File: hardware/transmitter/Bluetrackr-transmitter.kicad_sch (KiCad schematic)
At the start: 43 parts, among them J1 USB_C_Receptacle_USB2.0, J2 Programming_Connector, J3 Battery_Connector, Q1 CJ2333, SW1 SW_Pair, U1 MCP73831-2-OT, U2 MIC5205-2.5YM5, U4 STM32F030R8Tx

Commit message: Annotate schematic
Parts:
- gave numbers to parts that had none: 7
- renumbered C4 to C1, C13 to C10, C14 to C11, C9 to C12, C5 to C2, C2 to C3, C6 to C4, C1 to C5, C3 to C6, C10 to C7, C11 to C8, C12 to C9, R4 to R1, R5 to R2, R6 to R3, R1 to R4, R2 to R5, R3 to R6, U2 to U1, U1 to U2, U4 to U3

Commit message: Remove pcb
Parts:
- C12: footprint Capacitor_SMD:CP_Elec_4x5.4 -> Capacitor_SMD:CP_Elec_3x5.3
- C13, C14, C16, C17: footprint (none) -> Capacitor_SMD:C_0805_2012Metric_Pad1.15x1.40mm_HandSolder
- C15: footprint (none) -> Capacitor_SMD:CP_Elec_3x5.3
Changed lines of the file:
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@@
       (effects (font (size 1.27 1.27)) (justify left))
     )
-    (property "Footprint" "Capacitor_SMD:CP_Elec_4x5.4" (id 2) (at 205.4352 55.88 0)
+    (property "Footprint" "Capacitor_SMD:CP_Elec_3x5.3" (id 2) (at 205.4352 55.88 0)
       (effects (font (size 1.27 1.27)) hide)
     )
@@
       (effects (font (size 1.27 1.27)) (justify left))
     )
-    (property "Footprint" "" (id 2) (at 285.4452 85.09 0)
+    (property "Footprint" "Capacitor_SMD:C_0805_2012Metric_Pad1.15x1.40mm_HandSolder" (id 2) (at 285.4452 85.09 0)
       (effects (font (size 1.27 1.27)) hide)
     )
@@
       (effects (font (size 1.27 1.27)) (justify left))
     )
-    (property "Footprint" "" (id 2) (at 300.6852 85.09 0)
+    (property "Footprint" "Capacitor_SMD:C_0805_2012Metric_Pad1.15x1.40mm_HandSolder" (id 2) (at 300.6852 85.09 0)
       (effects (font (size 1.27 1.27)) hide)
     )
@@
       (effects (font (size 1.27 1.27)) (justify left))
     )
-    (property "Footprint" "" (id 2) (at 305.7652 118.11 0)
+    (property "Footprint" "Capacitor_SMD:CP_Elec_3x5.3" (id 2) (at 305.7652 118.11 0)
       (effects (font (size 1.27 1.27)) hide)
     )
@@
       (effects (font (size 1.27 1.27)) (justify left))
     )
-    (property "Footprint" "" (id 2) (at 315.9252 118.11 0)
+    (property "Footprint" "Capacitor_SMD:C_0805_2012Metric_Pad1.15x1.40mm_HandSolder" (id 2) (at 315.9252 118.11 0)
       (effects (font (size 1.27 1.27)) hide)
     )
@@
       (effects (font (size 1.27 1.27)) (justify left))
     )
-    (property "Footprint" "" (id 2) (at 327.3552 118.11 0)
+    (property "Footprint" "Capacitor_SMD:C_0805_2012Metric_Pad1.15x1.40mm_HandSolder" (id 2) (at 327.3552 118.11 0)
       (effects (font (size 1.27 1.27)) hide)
     )

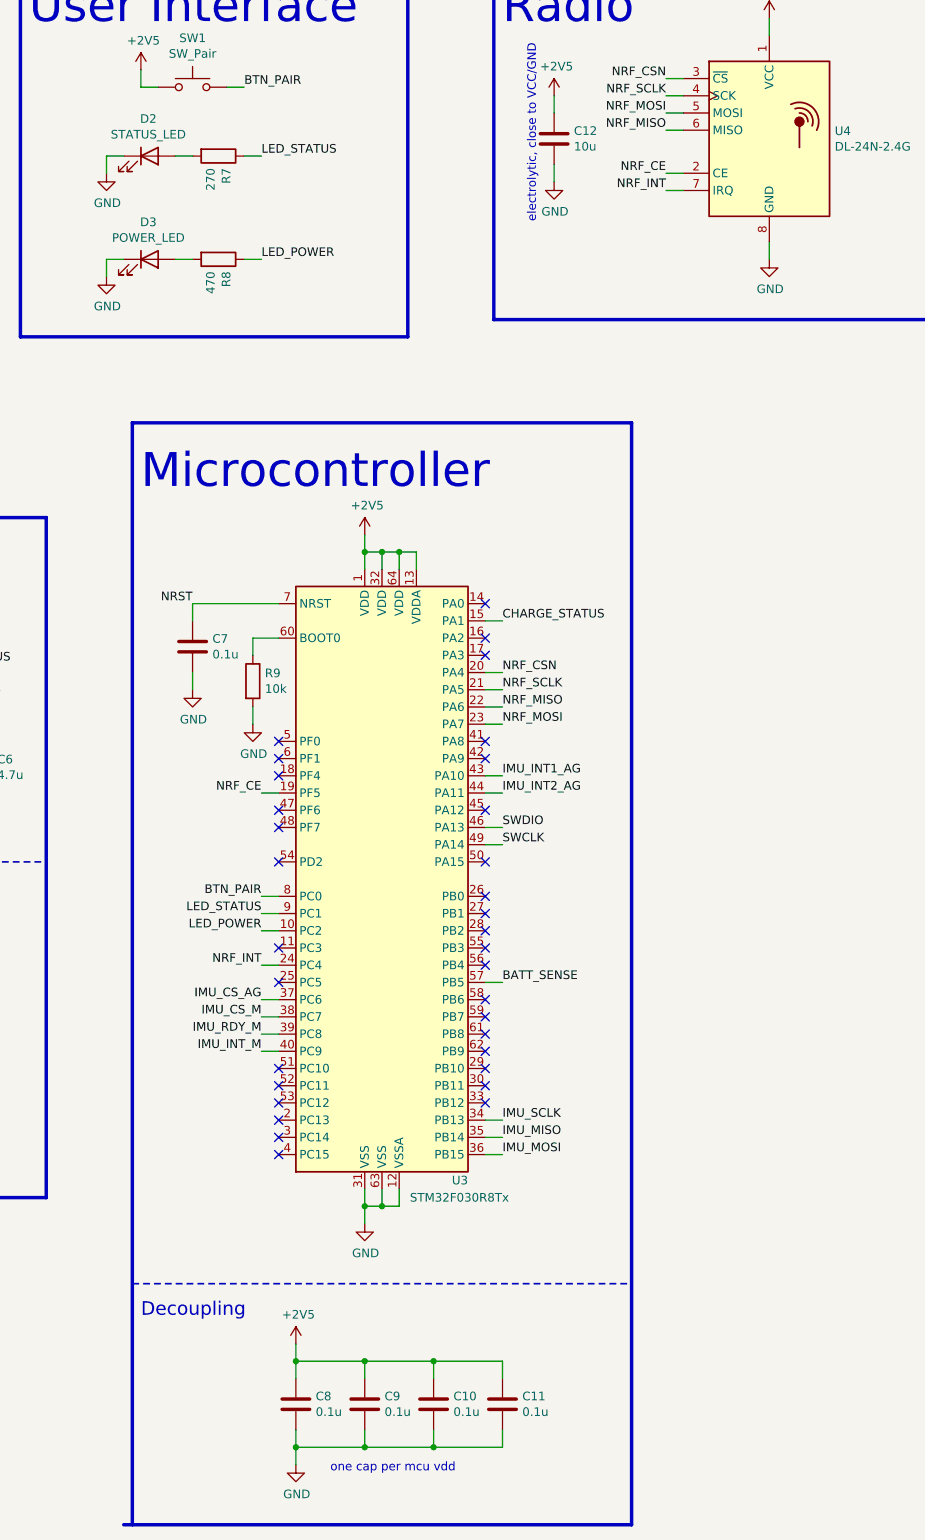
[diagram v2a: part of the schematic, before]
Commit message: Finish schematic with new Radio & IMU
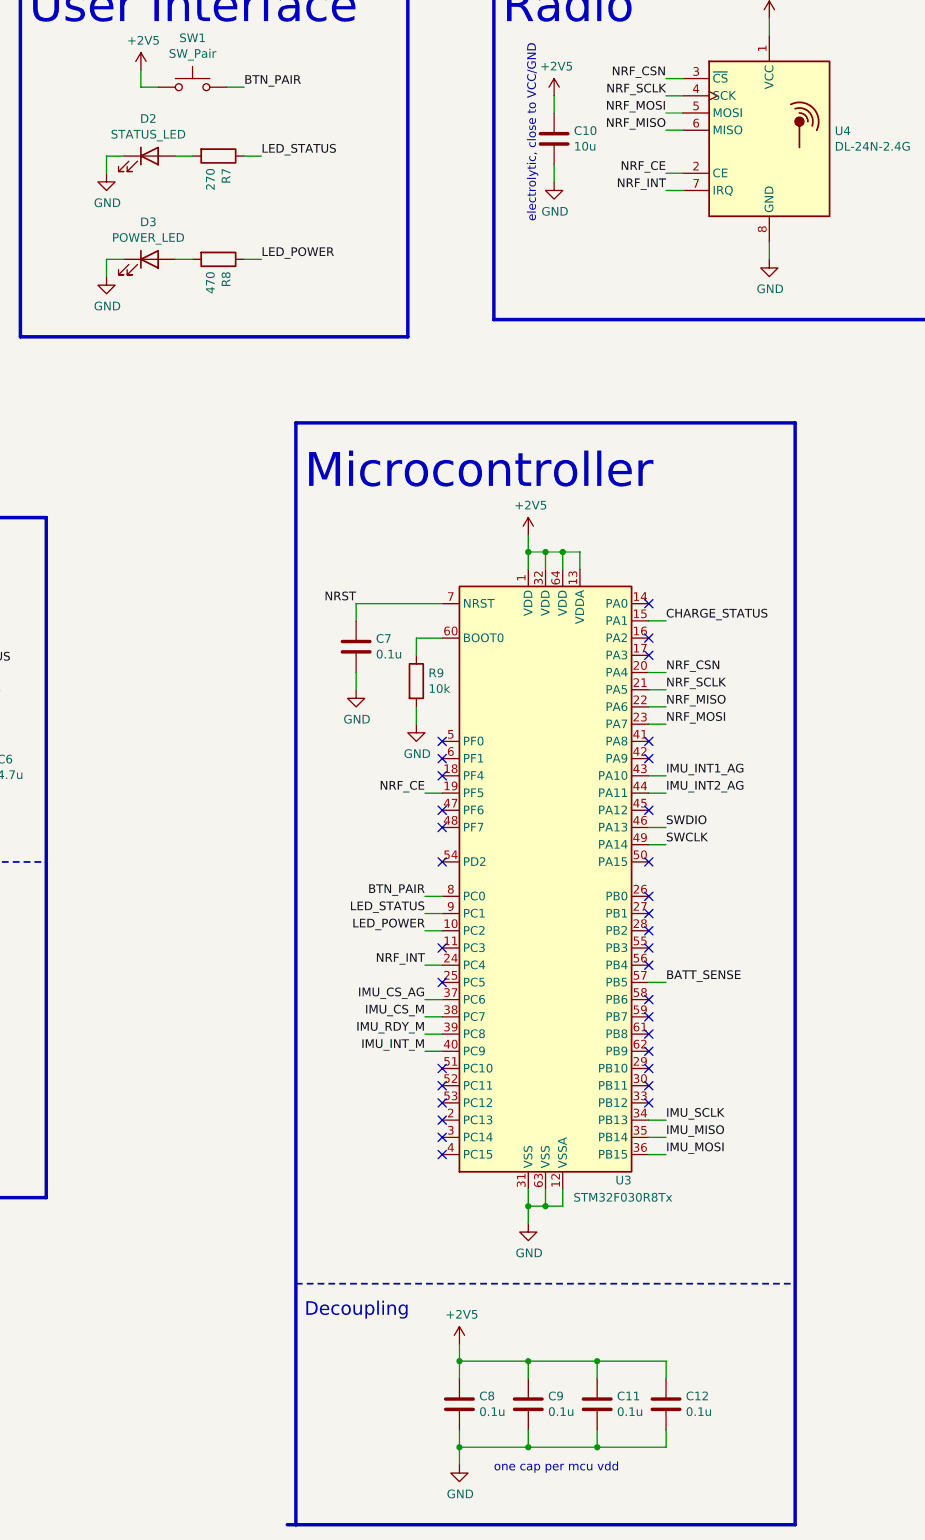
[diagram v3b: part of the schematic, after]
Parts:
- renumbered C12 to C10, C10 to C11, C11 to C12
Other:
- moved on the sheet: C11, C12, C7, C8, C9, R9, U3

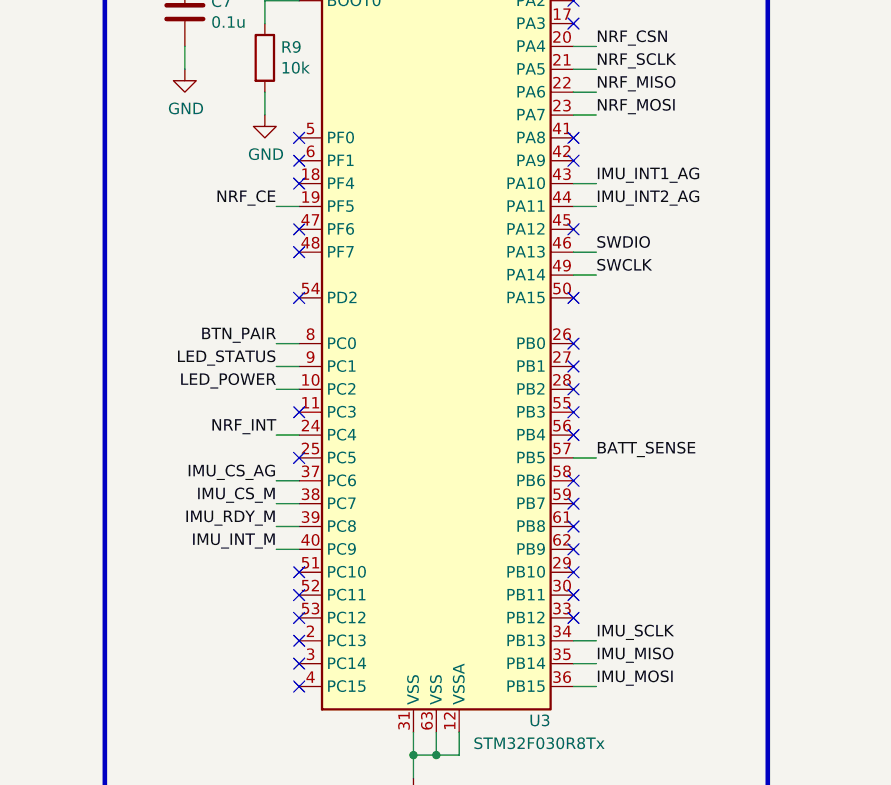
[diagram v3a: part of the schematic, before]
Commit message: Changed MCU to IMU pins
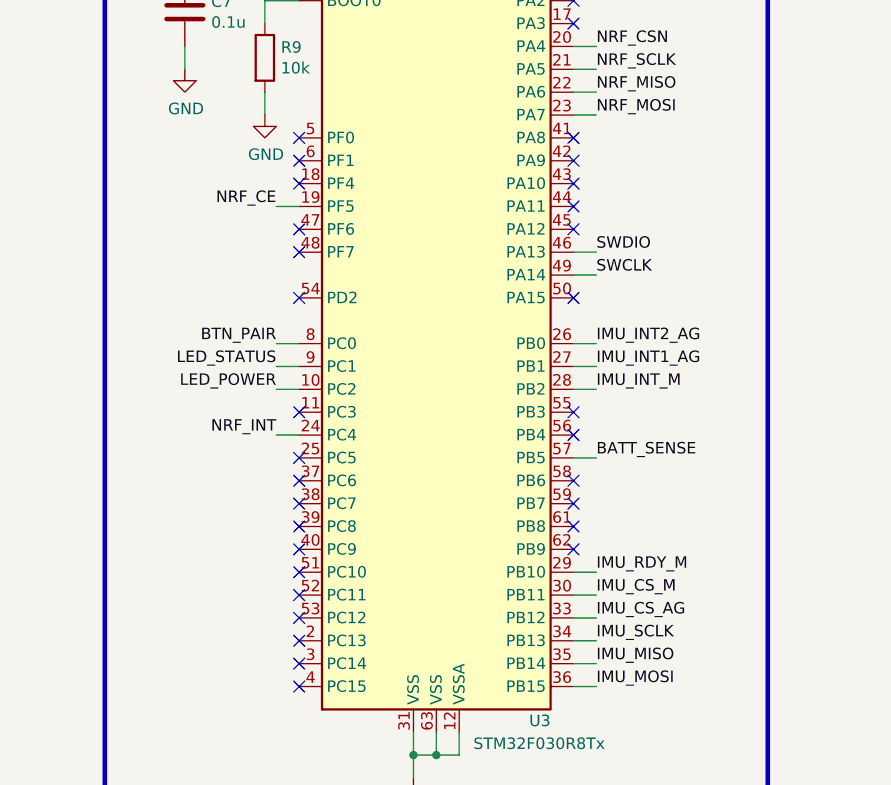
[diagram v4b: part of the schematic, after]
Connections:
- net IMU_CS_AG: now also U3.33 (PB12); no longer U3.37 (PC6)
- net IMU_CS_M: now also U3.30 (PB11); no longer U3.38 (PC7)
- net IMU_INT1_AG: now also U3.27 (PB1); no longer U3.43 (PA10)
- net IMU_INT2_AG: now also U3.26 (PB0); no longer U3.44 (PA11)
- net IMU_INT_M: now also U3.28 (PB2); no longer U3.40 (PC9)
- net IMU_RDY_M: now also U3.29 (PB10); no longer U3.39 (PC8)
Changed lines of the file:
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@@
   (junction (at 340.36 69.85))
   (junction (at 340.36 72.39))
-  (no_connect (at 218.44 189.23))
+  (no_connect (at 218.44 125.73))
+  (no_connect (at 187.96 196.85))
+  (no_connect (at 218.44 158.75))
+  (no_connect (at 54.61 58.42))
+  (no_connect (at 187.96 189.23))
+  (no_connect (at 187.96 153.67))
+  (no_connect (at 187.96 146.05))
+  (no_connect (at 187.96 140.97))
+  (no_connect (at 218.44 184.15))
+  (no_connect (at 218.44 186.69))
   (no_connect (at 218.44 151.13))
+  (no_connect (at 187.96 143.51))
+  (no_connect (at 54.61 60.96))
+  (no_connect (at 187.96 194.31))
+  (no_connect (at 218.44 181.61))
+  (no_connect (at 187.96 171.45))
+  (no_connect (at 218.44 143.51))
+  (no_connect (at 218.44 140.97))
+  (no_connect (at 187.96 191.77))
+  (no_connect (at 187.96 158.75))
+  (no_connect (at 54.61 66.04))
+  (no_connect (at 187.96 179.07))
+  (no_connect (at 187.96 181.61))
+  (no_connect (at 187.96 184.15))
+  (no_connect (at 187.96 186.69))
+  (no_connect (at 218.44 146.05))
+  (no_connect (at 218.44 148.59))
+  (no_connect (at 302.26 67.31))
+  (no_connect (at 54.61 63.5))
+  (no_connect (at 187.96 201.93))
   (no_connect (at 54.61 76.2))
-  (no_connect (at 187.96 153.67))
-  (no_connect (at 218.44 186.69))
+  (no_connect (at 218.44 128.27))
+  (no_connect (at 187.96 176.53))
+  (no_connect (at 218.44 171.45))
+  (no_connect (at 187.96 199.39))
+  (no_connect (at 187.96 151.13))
+  (no_connect (at 218.44 179.07))
+  (no_connect (at 218.44 120.65))
   (no_connect (at 54.61 73.66))
-  (no_connect (at 187.96 171.45))
-  (no_connect (at 187.96 201.93))
-  (no_connect (at 187.96 194.31))
-  (no_connect (at 218.44 191.77))
-  (no_connect (at 302.26 67.31))
-  (no_connect (at 187.96 176.53))
-  (no_connect (at 54.61 58.42))
-  (no_connect (at 187.96 191.77))
-  (no_connect (at 218.44 140.97))
-  (no_connect (at 187.96 158.75))
-  (no_connect (at 218.44 158.75))
-  (no_connect (at 187.96 140.97))
-  (no_connect (at 218.44 166.37))
-  (no_connect (at 218.44 120.65))
-  (no_connect (at 218.44 128.27))
-  (no_connect (at 54.61 63.5))
-  (no_connect (at 218.44 181.61))
-  (no_connect (at 218.44 163.83))
-  (no_connect (at 187.96 146.05))
-  (no_connect (at 218.44 194.31))
-  (no_connect (at 218.44 125.73))
-  (no_connect (at 218.44 168.91))
-  (no_connect (at 218.44 143.51))
-  (no_connect (at 187.96 199.39))
-  (no_connect (at 218.44 179.07))
-  (no_connect (at 187.96 151.13))
-  (no_connect (at 187.96 189.23))
-  (no_connect (at 218.44 184.15))
   (no_connect (at 218.44 173.99))
-  (no_connect (at 54.61 60.96))
-  (no_connect (at 187.96 143.51))
-  (no_connect (at 218.44 171.45))
-  (no_connect (at 54.61 66.04))
-  (no_connect (at 187.96 196.85))
   (wire (pts (xy 30.48 129.54) (xy 30.48 132.08))
     (stroke (width 0) (type solid) (color 0 0 0 0))
@@
     (stroke (width 0) (type solid) (color 0 0 0 0))
   )
-  (wire (pts (xy 185.42 179.07) (xy 187.96 179.07))
-    (stroke (width 0) (type solid) (color 0 0 0 0))
-  )
-  (wire (pts (xy 185.42 181.61) (xy 187.96 181.61))
-    (stroke (width 0) (type solid) (color 0 0 0 0))
-  )
-  (wire (pts (xy 185.42 184.15) (xy 187.96 184.15))
-    (stroke (width 0) (type solid) (color 0 0 0 0))
-  )
-  (wire (pts (xy 185.42 186.69) (xy 187.96 186.69))
-    (stroke (width 0) (type solid) (color 0 0 0 0))
-  )
   (wire (pts (xy 190.5 229.87) (xy 190.5 232.41))
     (stroke (width 0) (type solid) (color 0 0 0 0))
@@
     (stroke (width 0) (type solid) (color 0 0 0 0))
   )
-  (wire (pts (xy 218.44 146.05) (xy 220.98 146.05))
-    (stroke (width 0) (type solid) (color 0 0 0 0))
-  )
-  (wire (pts (xy 218.44 148.59) (xy 220.98 148.59))
-    (stroke (width 0) (type solid) (color 0 0 0 0))
-  )
   (wire (pts (xy 218.44 153.67) (xy 220.98 153.67))
     (stroke (width 0) (type solid) (color 0 0 0 0))
@@
     (stroke (width 0) (type solid) (color 0 0 0 0))
   )
+  (wire (pts (xy 218.44 163.83) (xy 220.98 163.83))
+    (stroke (width 0) (type solid) (color 0 0 0 0))
+  )
+  (wire (pts (xy 218.44 166.37) (xy 220.98 166.37))
+    (stroke (width 0) (type solid) (color 0 0 0 0))
+  )
+  (wire (pts (xy 218.44 168.91) (xy 220.98 168.91))
+    (stroke (width 0) (type solid) (color 0 0 0 0))
+  )
   (wire (pts (xy 218.44 176.53) (xy 220.98 176.53))
+    (stroke (width 0) (type solid) (color 0 0 0 0))
+  )
+  (wire (pts (xy 218.44 189.23) (xy 220.98 189.23))
+    (stroke (width 0) (type solid) (color 0 0 0 0))
+  )
+  (wire (pts (xy 218.44 191.77) (xy 220.98 191.77))
+    (stroke (width 0) (type solid) (color 0 0 0 0))
+  )
+  (wire (pts (xy 218.44 194.31) (xy 220.98 194.31))
     (stroke (width 0) (type solid) (color 0 0 0 0))
   )
@@
     (effects (font (size 1.27 1.27)) (justify right bottom))
   )
-  (label "IMU_CS_AG" (at 185.42 179.07 180)
-    (effects (font (size 1.27 1.27)) (justify right bottom))
-  )
-  (label "IMU_CS_M" (at 185.42 181.61 180)
-    (effects (font (size 1.27 1.27)) (justify right bottom))
-  )
-  (label "IMU_RDY_M" (at 185.42 184.15 180)
-    (effects (font (size 1.27 1.27)) (justify right bottom))
-  )
-  (label "IMU_INT_M" (at 185.42 186.69 180)
-    (effects (font (size 1.27 1.27)) (justify right bottom))
-  )
   (label "NRF_CSN" (at 220.98 43.18 180)
     (effects (font (size 1.27 1.27)) (justify right bottom))
@@
     (effects (font (size 1.27 1.27)) (justify left bottom))
   )
-  (label "IMU_INT1_AG" (at 220.98 146.05 0)
-    (effects (font (size 1.27 1.27)) (justify left bottom))
-  )
-  (label "IMU_INT2_AG" (at 220.98 148.59 0)
-    (effects (font (size 1.27 1.27)) (justify left bottom))
-  )
   (label "SWDIO" (at 220.98 153.67 0)
     (effects (font (size 1.27 1.27)) (justify left bottom))
@@
     (effects (font (size 1.27 1.27)) (justify left bottom))
   )
+  (label "IMU_INT2_AG" (at 220.98 163.83 0)
+    (effects (font (size 1.27 1.27)) (justify left bottom))
+  )
+  (label "IMU_INT1_AG" (at 220.98 166.37 0)
+    (effects (font (size 1.27 1.27)) (justify left bottom))
+  )
+  (label "IMU_INT_M" (at 220.98 168.91 0)
+    (effects (font (size 1.27 1.27)) (justify left bottom))
+  )
   (label "BATT_SENSE" (at 220.98 176.53 0)
     (effects (font (size 1.27 1.27)) (justify left bottom))
   )
+  (label "IMU_RDY_M" (at 220.98 189.23 0)
+    (effects (font (size 1.27 1.27)) (justify left bottom))
+  )
+  (label "IMU_CS_M" (at 220.98 191.77 0)
+    (effects (font (size 1.27 1.27)) (justify left bottom))
+  )
+  (label "IMU_CS_AG" (at 220.98 194.31 0)
+    (effects (font (size 1.27 1.27)) (justify left bottom))
+  )
